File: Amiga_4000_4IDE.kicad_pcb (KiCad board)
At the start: 2 copper layers, 71.1 x 58.7 mm, 11 parts, among them J1 AMIGA 4000, J2 CHANNEL 0, J3 CHANNEL 1

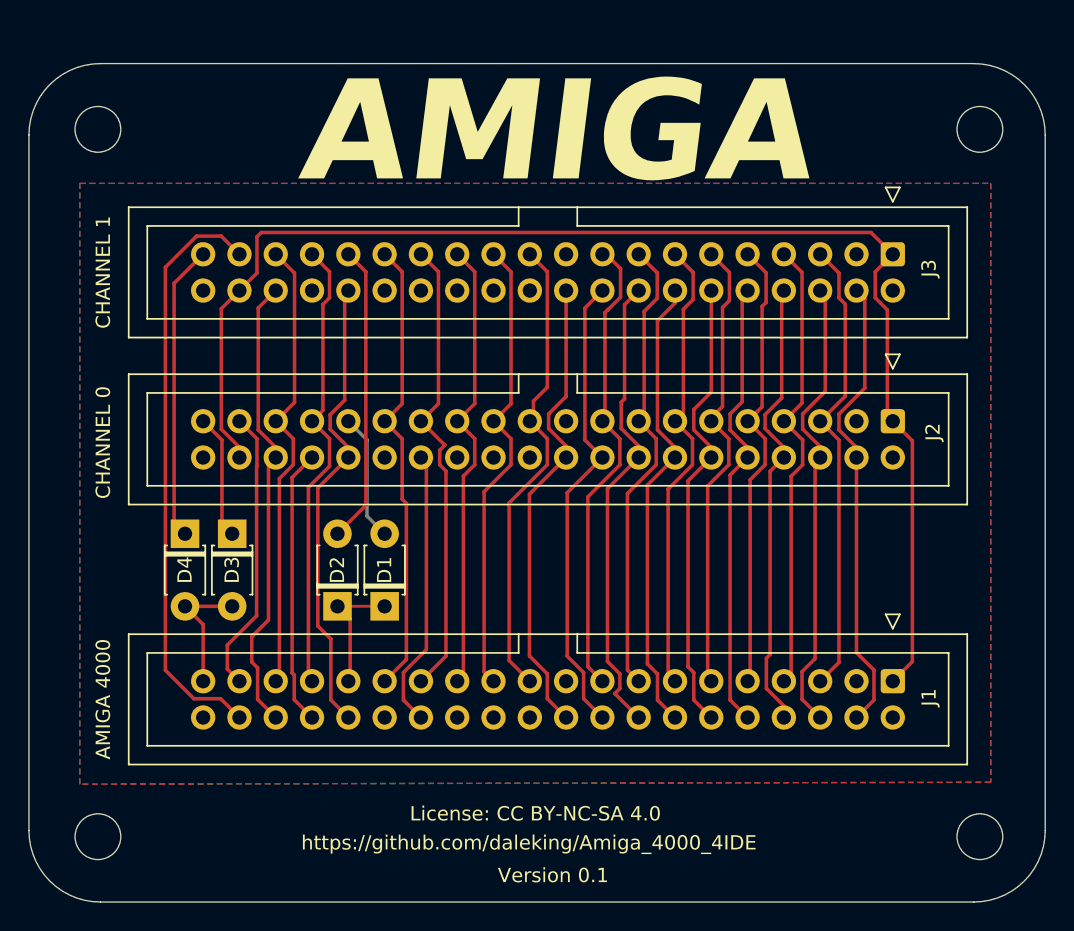
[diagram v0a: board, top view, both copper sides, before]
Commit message: Connect D7 (oops) and relayout PCB
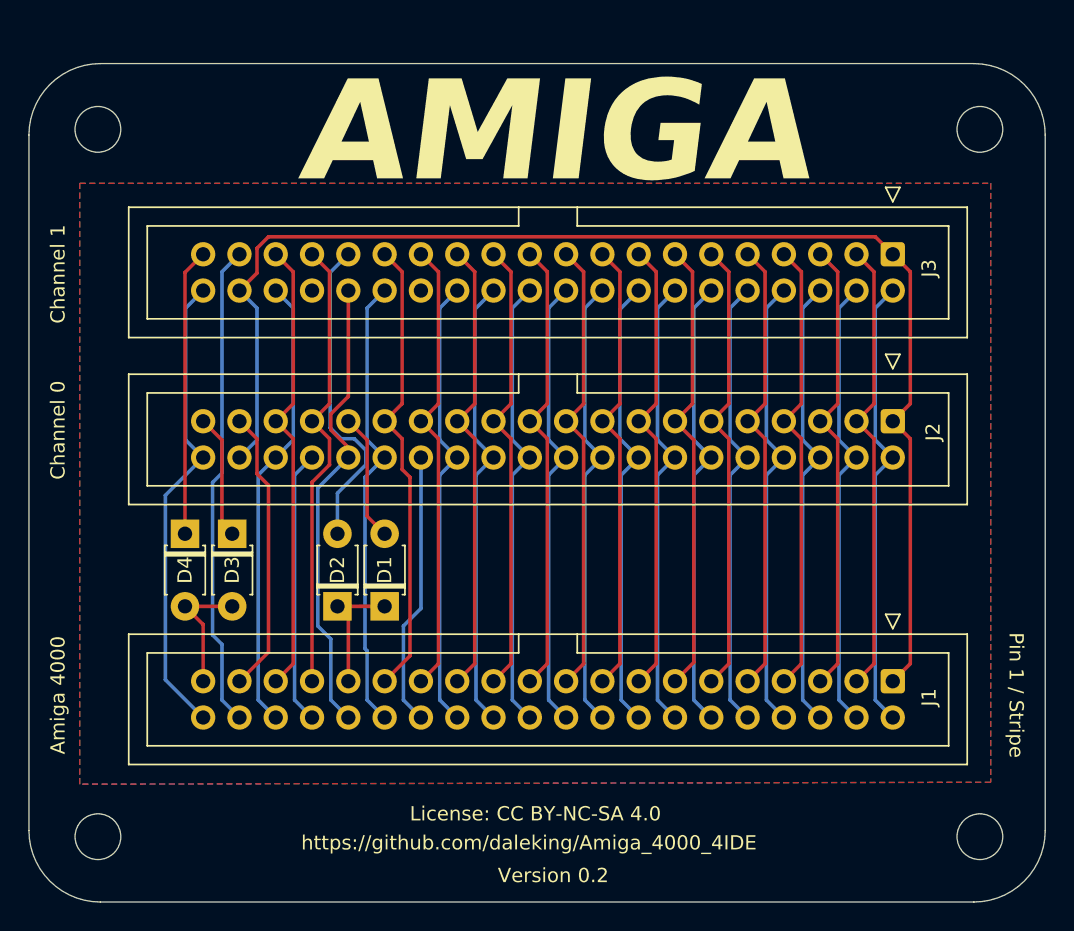
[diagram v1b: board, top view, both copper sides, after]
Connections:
- J1 pad 3: /VSS -> /D7
- J2 pad 3: /VSS -> /D7
- J3 pad 3: /VSS -> /D7
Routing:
- net /VSS: track 0.00 -> 224.7 mm
- net /D7: track 0.00 -> 31.9 mm
- net //IDE_CS2: track 41.4 -> 34.0 mm
- net /IRQ: track 5.66 -> 8.86 mm
- net Net-(D2-A): track 20.9 -> 22.5 mm
- net /nc21: track 33.1 -> 31.9 mm
- net /nc20: track 33.0 -> 31.9 mm
- net /D0: track 32.9 -> 31.9 mm
- net /D15: track 32.9 -> 31.9 mm
- net /D14: track 33.0 -> 32.0 mm
- net /DA1: track 32.8 -> 31.9 mm
- net //RESET: track 94.3 -> 93.4 mm
- net /IO_CH_RDY: track 32.6 -> 31.9 mm
- net /D1: track 32.6 -> 31.9 mm
- net Net-(D4-K): track 20.7 -> 20.1 mm
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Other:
- board text added: "Amiga 4000"
- board text added: "Channel 0"
- board text added: "Channel 1"
- board text added: "Pin 1 / Stripe"
- board text added: "Version 0.2"
- board text removed: "Version 0.1"
